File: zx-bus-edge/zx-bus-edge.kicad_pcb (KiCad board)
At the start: 2 copper layers, 71.3 x 16.7 mm, 2 parts

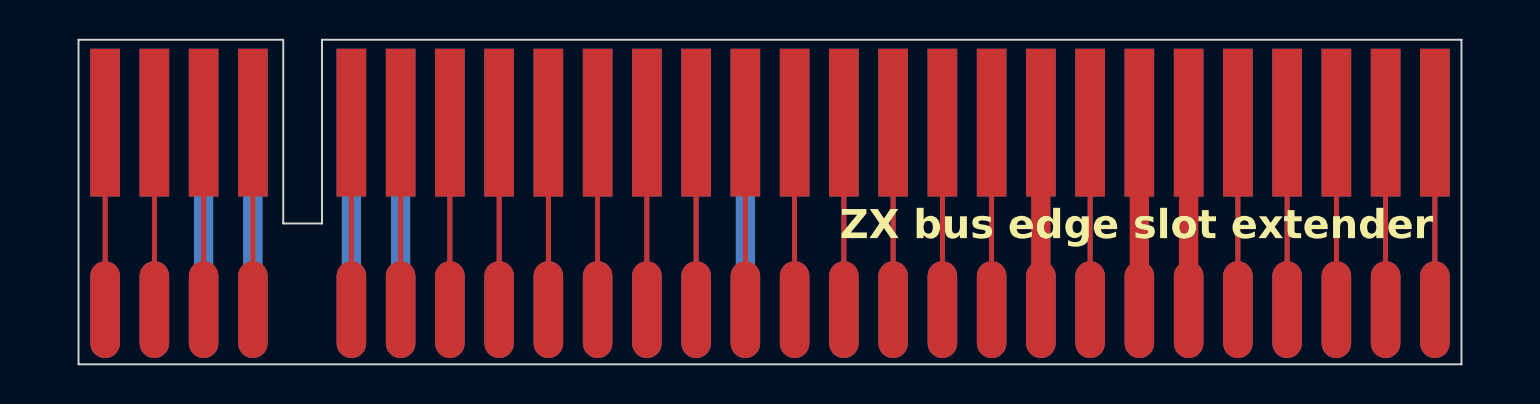
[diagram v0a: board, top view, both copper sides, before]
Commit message: Updated silk, fixed edge pcb dimensions a bit
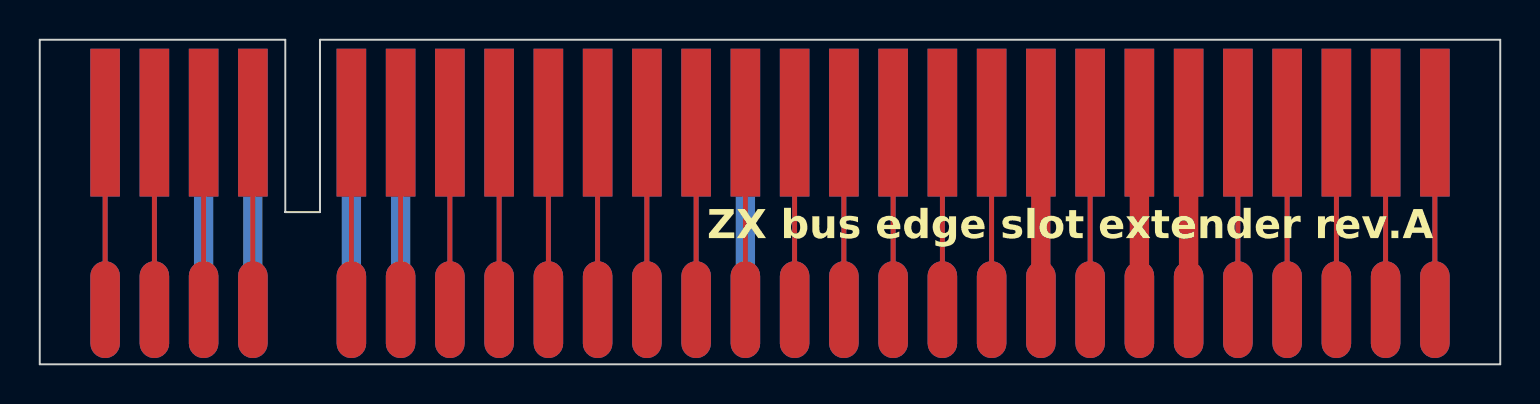
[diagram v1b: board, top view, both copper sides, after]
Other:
- board size 71.3 x 16.7 mm -> 75.3 x 16.7 mm
- board text added: "(c) andykarpov production 2024. Special exclusive Kalantaj edition"
- board text added: "ZX bus edge slot extender rev.A"
- board text removed: "ZX bus edge slot extender"
- board text removed: "andykarpov 2024"
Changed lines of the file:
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@@
 	)
 	(gr_line
-		(start 116.6716 122.4788)
-		(end 175.4378 122.4788)
+		(start 116.5653 122.4788)
+		(end 177.4378 122.4788)
 		(stroke
 			(width 0.1)
@@
 	)
 	(gr_line
-		(start 114.6716 131.953)
-		(end 114.6716 122.4788)
+		(start 114.7779 131.3688)
+		(end 114.7779 122.4788)
 		(stroke
 			(width 0.1)
@@
 	)
 	(gr_line
-		(start 175.4378 139.2174)
-		(end 104.1146 139.2174)
+		(start 177.4378 139.2174)
+		(end 102.1146 139.2174)
 		(stroke
 			(width 0.1)
@@
 	)
 	(gr_line
-		(start 116.6716 131.953)
-		(end 114.6716 131.953)
+		(start 116.5653 131.3688)
+		(end 114.7779 131.3688)
 		(stroke
 			(width 0.1)
@@
 	)
 	(gr_line
-		(start 114.6716 122.4788)
-		(end 104.1146 122.4788)
+		(start 114.7779 122.4788)
+		(end 102.1146 122.4788)
 		(stroke
 			(width 0.1)
@@
 	)
 	(gr_line
-		(start 116.6716 122.4788)
-		(end 116.6716 131.953)
+		(start 116.5653 122.4788)
+		(end 116.5653 131.3688)
 		(stroke
 			(width 0.1)
@@
 	)
 	(gr_line
-		(start 104.1146 139.2174)
-		(end 104.1146 122.4788)
+		(start 102.1146 139.2174)
+		(end 102.1146 122.4788)
 		(stroke
 			(width 0.1)
@@
 	)
 	(gr_line
-		(start 175.4378 122.4788)
-		(end 175.4378 139.2174)
+		(start 177.4378 122.4788)
+		(end 177.4378 139.2174)
 		(stroke
 			(width 0.1)
@@
 		(layer "Edge.Cuts")
 	)
-	(gr_text "andykarpov 2024"
+	(gr_text "(c) andykarpov production 2024. Special exclusive Kalantaj edition"
 		(at 174.0662 132.715 0)
 		(layer "B.SilkS")
@@
 		)
 	)
-	(gr_text "ZX bus edge slot extender\n"
+	(gr_text "ZX bus edge slot extender rev.A\n"
 		(at 173.99 132.8928 0)
 		(layer "F.SilkS")
@@
 		)
 	)
+	(dimension
+		(type aligned)
+		(layer "Dwgs.User")
+		(pts
+			(xy 114.7064 131.3688) (xy 114.7064 122.5296)
+		)
+		(height -6.505894)
+		(gr_text "8.8392 mm"
+			(at 107.050506 126.9492 90)
+			(layer "Dwgs.User")
+			(effects
+				(font
+					(size 1 1)
+					(thickness 0.15)
+				)
+			)
+		)
+		(format
+			(prefix "")
+			(suffix "")
+			(units 3)
+			(units_format 1)
+			(precision 4)
+		)
+		(style
+			(thickness 0.15)
+			(arrow_length 1.27)
+			(text_position_mode 0)
+			(extension_height 0.58642)
+			(extension_offset 0.5) keep_text_aligned)
+	)
+	(dimension
+		(type aligned)
+		(layer "Dwgs.User")
+		(pts
+			(xy 114.7826 130.9116) (xy 116.5352 130.9116)
+		)
+		(height 3.1496)
+		(gr_text "1.7526 mm"
+			(at 115.6589 132.9112 0)
+			(layer "Dwgs.User")
+			(effects
+				(font
+					(size 1 1)
+					(thickness 0.15)
+				)
+			)
+		)
+		(format
+			(prefix "")
+			(suffix "")
+			(units 3)
+			(units_format 1)
+			(precision 4)
+		)
+		(style
+			(thickness 0.15)
+			(arrow_length 1.27)
+			(text_position_mode 0)
+			(extension_height 0.58642)
+			(extension_offset 0.5) keep_text_aligned)
+	)
 	(segment
